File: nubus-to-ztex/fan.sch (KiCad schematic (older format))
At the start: 2 parts, among them J7 640456-3 (Fan)

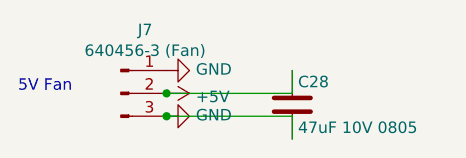
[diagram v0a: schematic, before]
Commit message: more THT->SMT, lexx expensive parts/assembly (?)
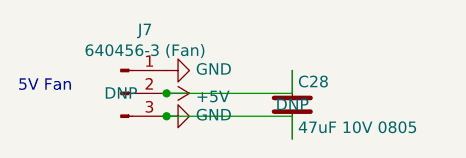
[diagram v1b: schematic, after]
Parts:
- C28, J7: DNP (none) -> DNP
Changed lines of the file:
@@
 F 8 "TE Connectivity" H 4400 4750 50  0001 C CNN "Manufacturer"
 F 9 "https://www.lcsc.com/product-detail/Wire-To-Board-Wire-To-Wire-Connector_TE-Connectivity-640456-3_C86503.html" H 4400 4750 50  0001 C CNN "URL"
+F 10 "DNP" H 4400 4750 50  0000 C CNN "DNP"
 	1    4400 4750
 	1    0    0    -1
@@
 F 6 "GRM21BR61A476ME15K" H 5150 4800 50  0001 C CNN "MPN"
 F 7 "https://www.lcsc.com/product-detail/Multilayer-Ceramic-Capacitors-MLCC-SMD-SMT_Murata-Electronics-GRM21BR61A476ME15K_C2292827.html" H 5150 4800 50  0001 C CNN "URL"
+F 8 "DNP" H 5150 4800 50  0000 C CNN "DNP"
 	1    5150 4800
 	1    0    0    -1

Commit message: BoM, power plane, serial back to THT, ...
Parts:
- C28: MPN GRM21BR61A476ME15K -> C2012X5R1A476MTJ00E; URL https://www.lcsc.com/product-detail/Multilayer-Ceramic-Capacitors-MLCC-SMD-SMT_Murata-Electronics-GRM21BR61A476ME15K_C2292827.html -> https://www.lcsc.com/product-detail/Multilayer-Ceramic-Capacitors-MLCC-SMD-SMT_TDK-C2012X5R1A476MTJ00E_C76636.html
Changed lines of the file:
@@
 F 4 "C2012X5R1A476MTJ00E" H 5150 4800 50  0001 C CNN "MPN-ALT"
 F 5 "https://lcsc.com/product-detail/Multilayer-Ceramic-Capacitors-MLCC-SMD-SMT_TDK-C2012X5R1A476MTJ00E_C76636.html" H 5150 4800 50  0001 C CNN "URL-ALT"
-F 6 "GRM21BR61A476ME15K" H 5150 4800 50  0001 C CNN "MPN"
-F 7 "https://www.lcsc.com/product-detail/Multilayer-Ceramic-Capacitors-MLCC-SMD-SMT_Murata-Electronics-GRM21BR61A476ME15K_C2292827.html" H 5150 4800 50  0001 C CNN "URL"
+F 6 "C2012X5R1A476MTJ00E" H 5150 4800 50  0001 C CNN "MPN"
+F 7 "https://www.lcsc.com/product-detail/Multilayer-Ceramic-Capacitors-MLCC-SMD-SMT_TDK-C2012X5R1A476MTJ00E_C76636.html" H 5150 4800 50  0001 C CNN "URL"
 F 8 "DNP" H 5150 4800 50  0000 C CNN "DNP"
 	1    5150 4800

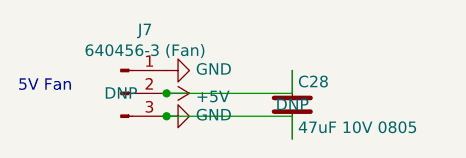
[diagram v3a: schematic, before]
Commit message: even more JLCPCB BoM optimization
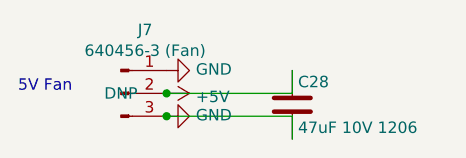
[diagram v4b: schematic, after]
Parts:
- C28: value 47uF 10V 0805 -> 47uF 10V 1206; footprint Capacitor_SMD:C_0805_2012Metric -> Capacitor_SMD:C_1206_3216Metric; DNP DNP -> (none); MPN C2012X5R1A476MTJ00E -> CL31A476MPHNNNE; URL https://www.lcsc.com/product-detail/Multilayer-Ceramic-Capacitors-MLCC-SMD-SMT_TDK-C2012X5R1A476MTJ00E_C76636.html -> https://www.lcsc.com/product-detail/Multilayer-Ceramic-Capacitors-MLCC-SMD-SMT_Samsung-Electro-Mechanics-CL31A476MPHNNNE_C96123.html
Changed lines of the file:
@@
 AR Path="/61B99D2C/60E24715" Ref="C28"  Part="1"
 F 0 "C28" H 5175 4900 50  0000 L CNN
-F 1 "47uF 10V 0805" H 5175 4700 50  0000 L CNN
-F 2 "Capacitor_SMD:C_0805_2012Metric" H 5188 4650 50  0001 C CNN
+F 1 "47uF 10V 1206" H 5175 4700 50  0000 L CNN
+F 2 "Capacitor_SMD:C_1206_3216Metric" H 5188 4650 50  0001 C CNN
 F 3 "" H 5150 4800 50  0000 C CNN
 F 4 "C2012X5R1A476MTJ00E" H 5150 4800 50  0001 C CNN "MPN-ALT"
 F 5 "https://lcsc.com/product-detail/Multilayer-Ceramic-Capacitors-MLCC-SMD-SMT_TDK-C2012X5R1A476MTJ00E_C76636.html" H 5150 4800 50  0001 C CNN "URL-ALT"
-F 6 "C2012X5R1A476MTJ00E" H 5150 4800 50  0001 C CNN "MPN"
-F 7 "https://www.lcsc.com/product-detail/Multilayer-Ceramic-Capacitors-MLCC-SMD-SMT_TDK-C2012X5R1A476MTJ00E_C76636.html" H 5150 4800 50  0001 C CNN "URL"
-F 8 "DNP" H 5150 4800 50  0000 C CNN "DNP"
+F 6 "CL31A476MPHNNNE" H 5150 4800 50  0001 C CNN "MPN"
+F 7 "https://www.lcsc.com/product-detail/Multilayer-Ceramic-Capacitors-MLCC-SMD-SMT_Samsung-Electro-Mechanics-CL31A476MPHNNNE_C96123.html" H 5150 4800 50  0001 C CNN "URL"
 	1    5150 4800
 	1    0    0    -1
